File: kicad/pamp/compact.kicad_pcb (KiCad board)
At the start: 2 copper layers, 80 x 100 mm, 79 parts, among them J1 input, J2 Conn_01x02_Female, J3 output, J4 power, Q1 2SA1381F, Q10 BC546B, Q11 MJE340, Q12 2SA1381F, Q13 2SC3503F, Q14 BC546B, Q15 BC556B, Q16 IRFP240N, Q17 IRFP9240N, Q2 2SC3503F, Q3 2SA1381F, Q4 2SC3503F, Q5 BC550C, Q6 BC560C, Q7 BC550C, Q8 BC560C, Q9 BC556B

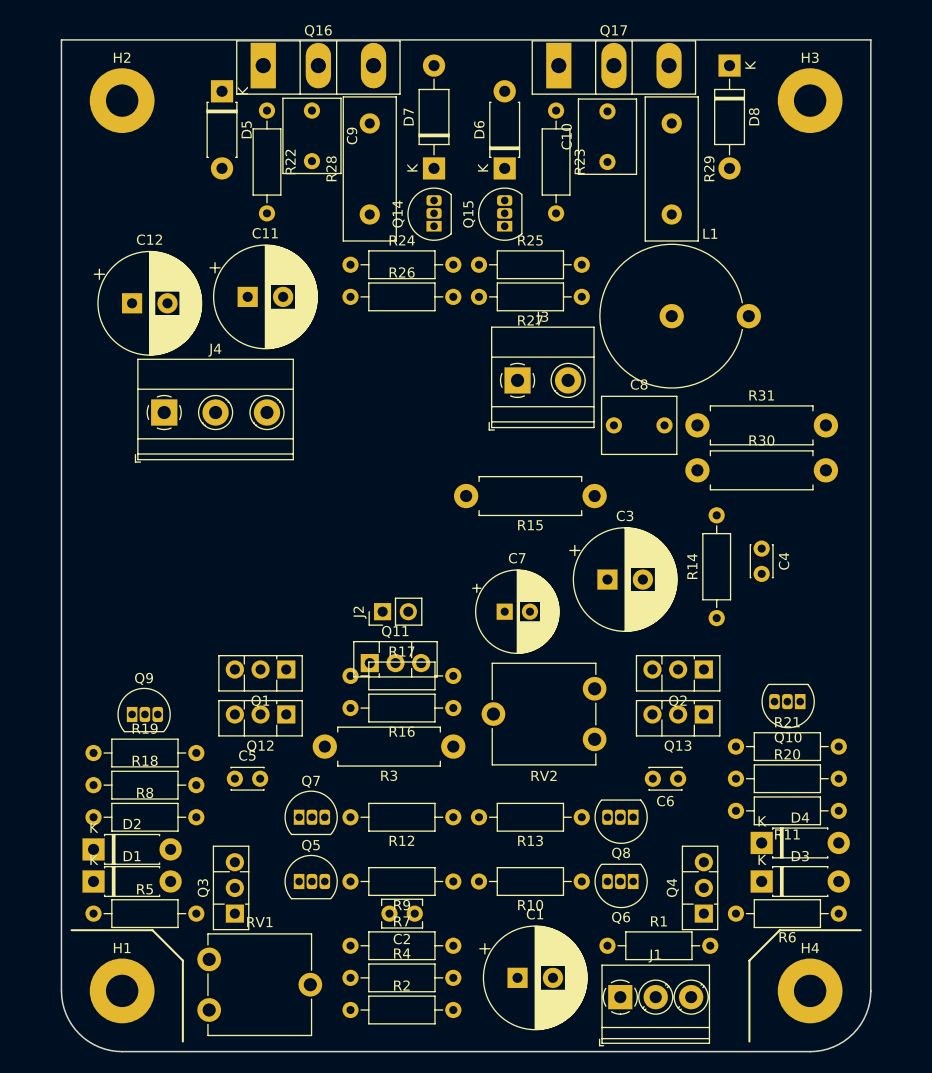
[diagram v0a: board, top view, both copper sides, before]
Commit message: Minimal PCB version.
Signed-off-by: Nenad Radulovic <nenad.b.radulovic@gmail.com>
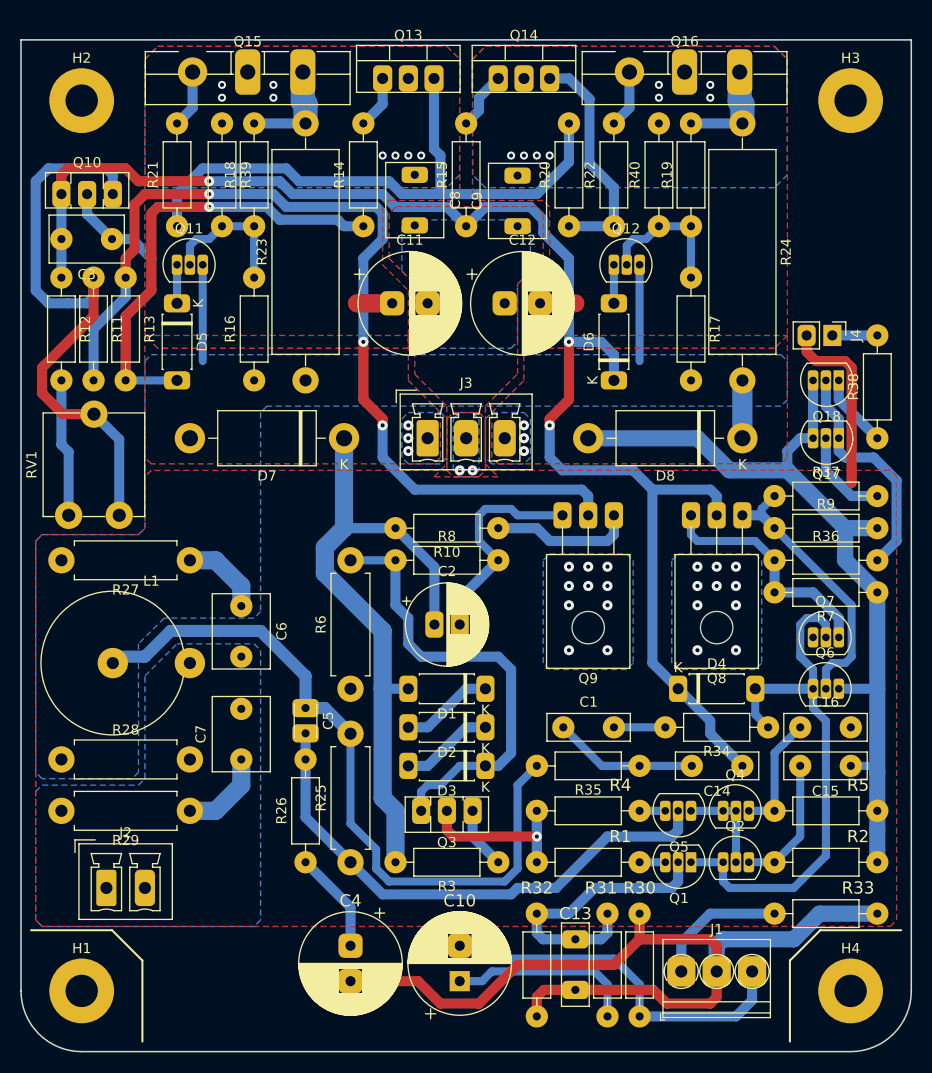
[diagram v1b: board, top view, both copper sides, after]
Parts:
- removed the C4 at (139.2, 80.3)
- removed the Q1 at (92.2, 92.2)
- removed the Q11 at (100.5, 91.6)
- removed the Q12 at (92.2, 96.7)
- removed the Q5 at (93.5, 113.2)
- removed the RV1 at (84.6, 125.9)
- added C13: 470p, Capacitor_THT:C_Disc_D8.0mm_W2.5mm_P5.00mm, F.Cu at (120.8, 123.9)
- added C14: 1n8, Capacitor_THT:C_Disc_D8.0mm_W2.5mm_P5.00mm, F.Cu at (137.3, 101.8)
- added C15: 220p, Capacitor_THT:C_Disc_D8.0mm_W2.5mm_P5.00mm, F.Cu at (148.0, 101.8)
- added C16: 220p, Capacitor_THT:C_Disc_D8.0mm_W2.5mm_P5.00mm, F.Cu at (143.0, 97.9)
- added C3: 220n, Capacitor_THT:C_Rect_L7.2mm_W4.5mm_P5.00mm_FKS2_FKP2_MKS2_MKP2, F.Cu at (75.0, 49.7)
- added Q14: Q_PNP_BCE, Package_TO_SOT_THT:TO-220-3_Vertical, F.Cu at (113.2, 33.8)
- added Q15: MJL3281, Package_TO_SOT_THT:TO-264-3_Vertical, F.Cu at (83.0, 33.2)
- added Q18: BC546B, Package_TO_SOT_THT:TO-92L_Inline, F.Cu at (146.8, 63.7)
- added Q6: BC546B, Package_TO_SOT_THT:TO-92L_Inline, F.Cu at (144.3, 94.1)
- added Q8: 2SC3503F, Package_TO_SOT_THT:TO-126-3_Horizontal_TabDown, F.Cu at (137.3, 77.0)
- added R32: 1k8, Resistor_THT:R_Axial_DIN0207_L6.3mm_D2.5mm_P10.16mm_Horizontal, F.Cu at (117.0, 126.5)
- added R33: 10, Resistor_THT:R_Axial_DIN0207_L6.3mm_D2.5mm_P10.16mm_Horizontal, F.Cu at (140.5, 116.4)
- added R34: 10, Resistor_THT:R_Axial_DIN0207_L6.3mm_D2.5mm_P10.16mm_Horizontal, F.Cu at (139.8, 97.9)
- added R35: 1k, Resistor_THT:R_Axial_DIN0207_L6.3mm_D2.5mm_P10.16mm_Horizontal, F.Cu at (127.1, 101.8)
- added R36: 10k, Resistor_THT:R_Axial_DIN0207_L6.3mm_D2.5mm_P10.16mm_Horizontal, F.Cu at (140.5, 81.4)
- added R37: 10k, Resistor_THT:R_Axial_DIN0207_L6.3mm_D2.5mm_P10.16mm_Horizontal, F.Cu at (140.5, 75.1)
- added R38: 10k, Resistor_THT:R_Axial_DIN0207_L6.3mm_D2.5mm_P10.16mm_Horizontal, F.Cu at (150.6, 69.4)
- added R39: 27k, Resistor_THT:R_Axial_DIN0207_L6.3mm_D2.5mm_P10.16mm_Horizontal, F.Cu at (85.9, 38.3)
- added R40: 27k, Resistor_THT:R_Axial_DIN0207_L6.3mm_D2.5mm_P10.16mm_Horizontal, F.Cu at (129.1, 48.4)
- C1: value 100u -> 180p; footprint Capacitor_THT:CP_Radial_D10.0mm_P3.50mm -> Capacitor_THT:C_Disc_D8.0mm_W2.5mm_P5.00mm
- C10: value 100n -> 100u; footprint Capacitor_THT:C_Rect_L7.2mm_W5.5mm_P5.00mm_FKS2_FKP2_MKS2_MKP2 -> Capacitor_THT:CP_Radial_D10.0mm_P3.50mm
- C2: value 470p -> 100u; footprint Capacitor_THT:C_Disc_D3.8mm_W2.6mm_P2.50mm -> Capacitor_THT:CP_Radial_D8.0mm_P2.50mm
- C5: value 47p -> 8.2p
- C6: value 47p -> 100n; footprint Capacitor_THT:C_Disc_D3.0mm_W2.0mm_P2.50mm -> Capacitor_THT:C_Rect_L7.2mm_W5.5mm_P5.00mm_FKS2_FKP2_MKS2_MKP2
- C7: value 47u -> 100n; footprint Capacitor_THT:CP_Radial_D8.0mm_P2.50mm -> Capacitor_THT:C_Rect_L7.2mm_W5.5mm_P5.00mm_FKS2_FKP2_MKS2_MKP2
- D7, D8: value ZPY12-TR -> 1N5401; footprint Diode_THT:D_DO-41_SOD81_P10.16mm_Horizontal -> Diode_THT:D_DO-201AD_P15.24mm_Horizontal
- J2: value Conn_01x02_Female -> output; footprint Connector_PinHeader_2.54mm:PinHeader_1x02_P2.54mm_Vertical -> Connector_Phoenix_MC:PhoenixContact_MCV_1,5_2-G-3.81_1x02_P3.81mm_Vertical
- J3: value output -> power; footprint TerminalBlock_Phoenix:TerminalBlock_Phoenix_MKDS-1,5-2_1x02_P5.00mm_Horizontal -> Connector_Phoenix_MC:PhoenixContact_MCV_1,5_3-G-3.81_1x03_P3.81mm_Vertical
- J4: value power -> Conn_01x02; footprint TerminalBlock_Phoenix:TerminalBlock_Phoenix_MKDS-1,5-3-5.08_1x03_P5.08mm_Horizontal -> Connector_PinHeader_2.54mm:PinHeader_1x02_P2.54mm_Vertical
- Q10: value BC546B -> MJE340; footprint Package_TO_SOT_THT:TO-92L_Inline -> Package_TO_SOT_THT:TO-126-3_Vertical
- Q13: value 2SC3503F -> 2SC4793; footprint Package_TO_SOT_THT:TO-126-3_Vertical -> Package_TO_SOT_THT:TO-220-3_Vertical
- Q16: value IRFP240N -> MJL1302; footprint Package_TO_SOT_THT:TO-247-3_Vertical -> Package_TO_SOT_THT:TO-264-3_Vertical
- Q17: value IRFP9240N -> BC546B; footprint Package_TO_SOT_THT:TO-247-3_Vertical -> Package_TO_SOT_THT:TO-92L_Inline
- Q2, Q4: value 2SC3503F -> BC550C; footprint Package_TO_SOT_THT:TO-126-3_Vertical -> Package_TO_SOT_THT:TO-92L_Inline
- Q7: value BC550C -> BC546B
- Q9: value BC556B -> 2SA1381F; footprint Package_TO_SOT_THT:TO-92L_Inline -> Package_TO_SOT_THT:TO-126-3_Horizontal_TabDown
- R1: value 10 -> 120
- R12, R4: value 100 -> 120
- R13: value 100 -> 33
- R14, R9: value 100 -> 24
- R15: value 1k5 -> 24; footprint Resistor_THT:R_Axial_DIN0411_L9.9mm_D3.6mm_P12.70mm_Horizontal -> Resistor_THT:R_Axial_DIN0207_L6.3mm_D2.5mm_P10.16mm_Horizontal
- R16: value 6k8 -> 330
- R17, R8: value 1k -> 330
- R18: value 18 -> 750
- R19: value 82 -> 750
- R2: value 10k -> 100
- R20: value 82 -> 62
- R21: value 18 -> 2R2
- R22: value 100 -> 2R2
- R23, R24: value 100 -> 0.22; footprint Resistor_THT:R_Axial_DIN0207_L6.3mm_D2.5mm_P10.16mm_Horizontal -> Resistor_THT:R_Axial_Power_L20.0mm_W6.4mm_P25.40mm
- R25: value 100 -> 1k8; footprint Resistor_THT:R_Axial_DIN0207_L6.3mm_D2.5mm_P10.16mm_Horizontal -> Resistor_THT:R_Axial_DIN0411_L9.9mm_D3.6mm_P12.70mm_Horizontal
- R27: value 100 -> 10; footprint Resistor_THT:R_Axial_DIN0207_L6.3mm_D2.5mm_P10.16mm_Horizontal -> Resistor_THT:R_Axial_DIN0411_L9.9mm_D3.6mm_P12.70mm_Horizontal
- R28: value 0.15 -> 4R7; footprint Resistor_THT:R_Box_L14.0mm_W5.0mm_P9.00mm -> Resistor_THT:R_Axial_DIN0411_L9.9mm_D3.6mm_P12.70mm_Horizontal
- R29: value 0.22 -> 10; footprint Resistor_THT:R_Box_L14.0mm_W5.0mm_P9.00mm -> Resistor_THT:R_Axial_DIN0411_L9.9mm_D3.6mm_P12.70mm_Horizontal
- R3: value 8k2 -> 330; footprint Resistor_THT:R_Axial_DIN0411_L9.9mm_D3.6mm_P12.70mm_Horizontal -> Resistor_THT:R_Axial_DIN0207_L6.3mm_D2.5mm_P10.16mm_Horizontal
- R30: value 10 -> 10k; footprint Resistor_THT:R_Axial_DIN0411_L9.9mm_D3.6mm_P12.70mm_Horizontal -> Resistor_THT:R_Axial_DIN0207_L6.3mm_D2.5mm_P10.16mm_Horizontal
- R31: value 4.7 -> 100; footprint Resistor_THT:R_Axial_DIN0411_L9.9mm_D3.6mm_P12.70mm_Horizontal -> Resistor_THT:R_Axial_DIN0207_L6.3mm_D2.5mm_P10.16mm_Horizontal
- R5: value 1k -> 100
- R6: value 560 -> 4k7; footprint Resistor_THT:R_Axial_DIN0207_L6.3mm_D2.5mm_P10.16mm_Horizontal -> Resistor_THT:R_Axial_DIN0411_L9.9mm_D3.6mm_P12.70mm_Horizontal
- R7: value 1k5 -> 910
- RV1: renamed from RV2; value R_POT_TRIM -> 500
- moved R11 90.6 mm to (73.2, 53.5), turned to 270 degrees
- moved Q10 88.6 mm to (70.0, 45.2), turned to 0 degrees
- moved R29 83.0 mm to (82.7, 106.2), turned to 180 degrees
- moved C10 82.3 mm to (109.4, 123.0)
- moved R19 78.7 mm to (132.2, 48.4), turned to 90 degrees
- moved R5 78.1 mm to (150.6, 106.2), turned to 180 degrees
- moved R21 75.5 mm to (81.4, 48.4), turned to 90 degrees
- moved Q13 70.4 mm to (101.7, 33.8), turned to 0 degrees
- moved R13 69.8 mm to (76.3, 53.5), turned to 270 degrees
- moved J4 66.5 mm to (146.2, 59.2), turned to 270 degrees
- moved R12 65.9 mm to (70.0, 53.5), turned to 270 degrees
- moved L1 65.0 mm to (75.1, 91.6)
- moved R7 62.7 mm to (150.6, 84.6), turned to 180 degrees
- moved R28 61.9 mm to (70.0, 101.1), turned to 0 degrees
- moved R25 60.4 mm to (98.6, 111.3), turned to 90 degrees
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- renumbered C3 to C4, Q6 to Q1, Q14 to Q11, Q15 to Q12, Q8 to Q5
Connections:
- C10 pad 1: GNDA -> Net-(C10-Pad1)
- C10 pad 2: VSS -> Net-(C10-Pad2)
- C2 pad 1: GNDS -> VDD
- C4 pad 1: Net-(C3-Pad1) -> Net-(C4-Pad1)
- C5 pad 2: Net-(C5-Pad2) -> inv
- C6 pad 2: Net-(C6-Pad2) -> GNDA
- C7 pad 1: Net-(C5-Pad2) -> Net-(C7-Pad1)
- C7 pad 2: Net-(C6-Pad1) -> GNDA
- C8 pad 1: Net-(C8-Pad1) -> VDD
- C9 pad 1: VDD -> GNDA
- C9 pad 2: GNDA -> VSS
- D3 pad 2: Net-(D3-Pad2) -> Net-(D2-Pad1)
- D4 pad 1: VSS -> Net-(C14-Pad1)
- D4 pad 2: Net-(D3-Pad1) -> Net-(D4-Pad2)
- D5 pad 2: Net-(C5-Pad2) -> Net-(C3-Pad1)
- D6 pad 1: Net-(C6-Pad1) -> Net-(C14-Pad1)
- D7 pad 1: Net-(D5-Pad1) -> VDD
- D7 pad 2: Net-(D7-Pad2) -> Net-(C5-Pad1)
- D8 pad 1: Net-(D8-Pad1) -> Net-(C5-Pad1)
- D8 pad 2: Net-(D6-Pad2) -> VSS
- J1 pad 3: Net-(C1-Pad2) -> Net-(C10-Pad2)
- J2 pad 2: Net-(C6-Pad1) -> GNDA
- J3 pad 1: Net-(J3-Pad1) -> VDD
- J4 pad 1: VDD -> Net-(J4-Pad1)
- L1 pad 1: Net-(C4-Pad1) -> Net-(C5-Pad1)
- L1 pad 2: Net-(J3-Pad1) -> Net-(J2-Pad1)
- Q1 pad 1: Net-(C6-Pad2) -> Net-(D4-Pad2)
- Q1 pad 2: Net-(C2-Pad2) -> ninv
- Q1 pad 3: Net-(Q6-Pad3) -> Net-(Q1-Pad3)
- Q10 pad 1: Net-(C6-Pad2) -> Net-(C14-Pad1)
- Q10 pad 2: Net-(Q10-Pad2) -> Net-(C3-Pad1)
- Q10 pad 3: VSS -> Net-(Q10-Pad3)
- Q11 pad 2: Net-(Q14-Pad2) -> Net-(Q11-Pad2)
- Q11 pad 3: Net-(C4-Pad1) -> Net-(C5-Pad1)
- Q12 pad 2: Net-(Q15-Pad2) -> Net-(Q12-Pad2)
- Q12 pad 3: Net-(C4-Pad1) -> Net-(C5-Pad1)
- Q13 pad 2: Net-(C6-Pad1) -> VDD
- Q13 pad 3: Net-(C6-Pad2) -> Net-(Q13-Pad3)
- Q16 pad 2: VDD -> VSS
- Q16 pad 3: Net-(D7-Pad2) -> Net-(Q16-Pad3)
- Q17 pad 2: VSS -> Net-(Q17-Pad2)
- Q17 pad 3: Net-(D8-Pad1) -> VSS
- Q2 pad 1: Net-(D3-Pad2) -> Net-(D4-Pad2)
- Q2 pad 3: Net-(Q2-Pad3) -> Net-(C15-Pad2)
- Q3 pad 1: Net-(Q1-Pad3) -> Net-(Q3-Pad1)
- Q3 pad 3: Net-(Q1-Pad2) -> Net-(D3-Pad1)
- Q4 pad 1: Net-(Q2-Pad3) -> Net-(Q2-Pad2)
- Q4 pad 2: Net-(Q4-Pad2) -> Net-(Q2-Pad2)
- Q4 pad 3: Net-(Q2-Pad2) -> Net-(C16-Pad1)
- Q5 pad 1: VSS -> Net-(Q2-Pad2)
- Q5 pad 2: Net-(C4-Pad2) -> inv
- Q5 pad 3: Net-(Q8-Pad3) -> Net-(Q5-Pad3)
- Q7 pad 1: VDD -> GNDA
- Q7 pad 2: Net-(C4-Pad2) -> Net-(D4-Pad2)
- Q9 pad 1: Net-(C5-Pad1) -> Net-(Q9-Pad1)
- Q9 pad 3: VDD -> Net-(C2-Pad2)
- R1 pad 1: GNDA -> Net-(Q1-Pad3)
- R1 pad 2: GNDS -> Net-(Q3-Pad2)
- R10 pad 1: Net-(Q6-Pad3) -> Net-(Q9-Pad1)
- R10 pad 2: Net-(Q3-Pad2) -> VDD
- R11 pad 1: VSS -> Net-(Q10-Pad3)
- R11 pad 2: Net-(C6-Pad2) -> Net-(Q9-Pad2)
- R12 pad 1: Net-(Q4-Pad2) -> Net-(C14-Pad1)
- R12 pad 2: Net-(Q7-Pad3) -> Net-(R12-Pad2)
- R13 pad 1: Net-(Q8-Pad3) -> Net-(Q9-Pad2)
- R13 pad 2: Net-(Q3-Pad2) -> Net-(C3-Pad1)
- R14 pad 1: Net-(C4-Pad2) -> Net-(C3-Pad1)
- R14 pad 2: Net-(C3-Pad1) -> Net-(Q13-Pad1)
- R15 pad 1: Net-(C4-Pad2) -> Net-(C14-Pad1)
- R15 pad 2: Net-(C4-Pad1) -> Net-(Q14-Pad1)
- R16 pad 1: Net-(Q11-Pad3) -> Net-(C5-Pad1)
- R16 pad 2: Net-(C5-Pad2) -> Net-(Q11-Pad2)
- R17 pad 1: Net-(C6-Pad1) -> Net-(Q12-Pad2)
- R17 pad 2: Net-(R17-Pad2) -> Net-(C5-Pad1)
- R18 pad 1: Net-(Q9-Pad2) -> Net-(Q11-Pad2)
- R18 pad 2: VDD -> Net-(Q15-Pad3)
- R19 pad 1: Net-(Q12-Pad1) -> Net-(Q12-Pad2)
- R19 pad 2: Net-(Q9-Pad2) -> Net-(Q16-Pad3)
- R2 pad 1: GNDS -> VSS
- R2 pad 2: Net-(C1-Pad2) -> Net-(C15-Pad2)
- R20 pad 1: Net-(Q10-Pad2) -> Net-(Q14-Pad3)
- R20 pad 2: Net-(Q13-Pad1) -> Net-(Q13-Pad3)
- R21 pad 1: VSS -> Net-(Q13-Pad3)
- R21 pad 2: Net-(Q10-Pad2) -> Net-(Q15-Pad1)
- R22 pad 1: Net-(Q16-Pad1) -> Net-(Q14-Pad3)
- R22 pad 2: Net-(C5-Pad2) -> Net-(Q16-Pad1)
- R23 pad 1: Net-(Q17-Pad1) -> Net-(C5-Pad1)
- R23 pad 2: Net-(C6-Pad1) -> Net-(Q15-Pad3)
- R24 pad 1: Net-(C4-Pad1) -> Net-(Q16-Pad3)
- R24 pad 2: Net-(Q14-Pad2) -> Net-(C5-Pad1)
- R25 pad 1: Net-(Q15-Pad2) -> inv
- R25 pad 2: Net-(C4-Pad1) -> Net-(C5-Pad1)
- R26 pad 1: Net-(D7-Pad2) -> Net-(C4-Pad1)
- R26 pad 2: Net-(Q14-Pad2) -> inv
- R27 pad 1: Net-(D8-Pad1) -> Net-(C6-Pad1)
- R27 pad 2: Net-(Q15-Pad2) -> Net-(C5-Pad1)
- R28 pad 1: Net-(C4-Pad1) -> Net-(C5-Pad1)
- R28 pad 2: Net-(D7-Pad2) -> Net-(J2-Pad1)
- R29 pad 1: Net-(D8-Pad1) -> Net-(C7-Pad1)
- R29 pad 2: Net-(C4-Pad1) -> Net-(J2-Pad1)
- R3 pad 1: Net-(Q2-Pad2) -> Net-(Q3-Pad1)
- R3 pad 2: Net-(Q1-Pad2) -> VDD
- R30 pad 1: Net-(C8-Pad1) -> GNDS
- R30 pad 2: Net-(C4-Pad1) -> Net-(C10-Pad2)
- R31 pad 1: Net-(C4-Pad1) -> Net-(C10-Pad1)
- R31 pad 2: Net-(J3-Pad1) -> ninv
- R4 pad 1: Net-(C2-Pad2) -> Net-(Q5-Pad3)
- R4 pad 2: Net-(C1-Pad1) -> Net-(Q3-Pad2)
- R5 pad 1: Net-(Q1-Pad3) -> VSS
- R5 pad 2: Net-(R5-Pad2) -> Net-(C16-Pad1)
- R6 pad 1: VSS -> GNDA
- R6 pad 2: Net-(Q2-Pad3) -> Net-(D3-Pad1)
- R7 pad 1: Net-(C2-Pad2) -> VSS
- R7 pad 2: GNDS -> Net-(Q7-Pad3)
- R8 pad 1: Net-(C5-Pad1) -> Net-(D3-Pad1)
- R8 pad 2: VDD -> Net-(C2-Pad2)
- R9 pad 1: Net-(Q4-Pad2) -> Net-(Q6-Pad2)
- R9 pad 2: Net-(Q5-Pad3) -> VSS
- RV1 pad 1: Net-(Q11-Pad3) -> Net-(Q10-Pad3)
- RV1 pad 2: Net-(Q11-Pad3) -> Net-(Q10-Pad3)
- RV1 pad 3: Net-(R17-Pad2) -> Net-(R12-Pad2)
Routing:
- net Net-(C14-Pad1): track 0.00 -> 145.6 mm, vias 0 -> 3
- net Net-(C5-Pad1): track 0.00 -> 95.7 mm
- net Net-(Q9-Pad2): track 0.00 -> 94.3 mm, vias 0 -> 3
- net GNDS: track 0.00 -> 88.2 mm
- net VSS: track 0.00 -> 87.2 mm, vias 0 -> 11
- net Net-(C3-Pad1): track 0.00 -> 67.9 mm, vias 0 -> 1
- net VDD: track 0.00 -> 67.8 mm, vias 0 -> 11
- net Net-(Q13-Pad3): track 0.00 -> 60.8 mm
- net Net-(Q10-Pad3): track 0.00 -> 60.1 mm
- net Net-(D4-Pad2): track 0.00 -> 55.1 mm
- net inv: track 0.00 -> 52.8 mm
- net Net-(D3-Pad1): track 0.00 -> 45.1 mm
- net Net-(C10-Pad2): track 0.00 -> 37.2 mm
- net GNDA: track 0.00 -> 31.4 mm, vias 0 -> 22
- net ninv: track 0.00 -> 28.5 mm
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- added copper zone on B.Cu, net GNDA
- added copper zone on F.Cu, net GNDA
- added copper zone on B.Cu, net Net-(C5-Pad1)
- added copper zone on B.Cu, net Net-(J2-Pad1)
- added copper zone on B.Cu, net VDD
- added copper zone on F.Cu, net VDD
- added copper zone on B.Cu, net VSS
- added copper zone on F.Cu, net VSS
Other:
- board size 80 x 100 mm -> 88 x 100 mm
- net class Default: clearance 0.2 -> 0.2032; trace_width 0.25 -> 0.3; via_dia 0.8 -> 1
- rule trace_clearance: 0.2 -> 0.2032
- rule trace_min: 0.2 -> 0.3

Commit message: First prerelease.
Signed-off-by: Nenad Radulovic <nenad.b.radulovic@gmail.com>
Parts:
- removed the C1 at (119.6, 97.9)
- removed the C14 at (137.3, 101.8)
- removed the C16 at (143.0, 97.9)
- removed Q17, Q18: BC546B, Package_TO_SOT_THT:TO-92L_Inline
- removed the R12 at (70.0, 53.5)
- removed the R17 at (132.2, 53.5)
- removed the R18 at (89.0, 48.4)
- removed the R19 at (132.2, 48.4)
- removed the R23 at (94.1, 63.7)
- removed the R34 at (139.8, 97.9)
- removed R35: 1k, Resistor_THT:R_Axial_DIN0207_L6.3mm_D2.5mm_P10.16mm_Horizontal
- removed R39, R40: 27k, Resistor_THT:R_Axial_DIN0207_L6.3mm_D2.5mm_P10.16mm_Horizontal
- added C2: 220p, Capacitor_THT:C_Disc_D8.0mm_W2.5mm_P5.00mm, F.Cu at (143.1, 99.8)
- added C3: 180p, Capacitor_THT:C_Disc_D8.0mm_W2.5mm_P5.00mm, F.Cu at (125.2, 88.4)
- added C5: 1n8, Capacitor_THT:C_Disc_D8.0mm_W2.5mm_P5.00mm, F.Cu at (125.2, 78.3)
- added D6: BAV21, Diode_THT:D_DO-41_SOD81_P7.62mm_Horizontal, F.Cu at (89.0, 59.2)
- added D7: BAV21, Diode_THT:D_DO-41_SOD81_P7.62mm_Horizontal, F.Cu at (124.6, 59.2)
- added LOGO1: Logo_Open_Hardware_Small, Symbol:KiCad-Logo_5mm_Copper, F.Cu at (86.0, 123.0)
- added R11: 1k, Resistor_THT:R_Axial_DIN0207_L6.3mm_D2.5mm_P10.16mm_Horizontal, F.Cu at (126.5, 97.9)
- added R25: 0.22, Resistor_THT:R_Axial_Power_L20.0mm_W6.4mm_P25.40mm, F.Cu at (137.3, 38.3)
- added R7: 10, Resistor_THT:R_Axial_DIN0207_L6.3mm_D2.5mm_P10.16mm_Horizontal, F.Cu at (139.8, 97.9)
- Q1, Q11, Q2, Q4, Q5, Q6, Q7: footprint Package_TO_SOT_THT:TO-92L_Inline -> Package_TO_SOT_THT:TO-92L_Inline_Wide
- Q12: value BC556B -> BC546B; footprint Package_TO_SOT_THT:TO-92L_Inline -> Package_TO_SOT_THT:TO-92L_Inline_Wide
- R16: value 330 -> 120
- moved Q11 68.8 mm to (148.1, 69.4), turned to 180 degrees
- moved R24 50.1 mm to (94.1, 63.7), turned to 90 degrees
- moved Q12 26.1 mm to (148.1, 63.7), turned to 180 degrees
- moved R16 21.6 mm to (70.0, 53.5), turned to 270 degrees
- moved D4 16.1 mm to (128.4, 78.3), turned to 270 degrees
- moved D8 12.7 mm to (132.2, 53.5), turned to 180 degrees
- moved R18 10.2 mm to (150.6, 59.2)
- moved C1 5.72 mm to (148.0, 107.5)
- moved Q9 3.42 mm to (121.4, 78.3)
- moved Q1 2.84 mm to (131.0, 113.8), turned to 90 degrees
- moved R4 2.62 mm to (126.5, 103.7)
- moved Q2 2.62 mm to (136.0, 113.8), turned to 90 degrees
- moved R5 2.54 mm to (150.6, 103.7)
- moved D5 2.54 mm to (81.4, 53.5), turned to 0 degrees
- moved Q8 1.27 mm to (137.3, 78.3)
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- renumbered C15 to C1, C7 to C10, C8 to C11, C9 to C12, C10 to C13, C11 to C14, C12 to C15, C13 to C16, C2 to C4, C3 to C6, C4 to C7, C5 to C8, C6 to C9, D8 to D10, D6 to D8, D7 to D9, J4 to J1, J1 to J2, J2 to J3, J3 to J4, R9 to R10, R36 to R12, R37 to R13, R10 to R14, R11 to R15, R13 to R17, R38 to R18, R14 to R19, R15 to R20, R20 to R21, R21 to R22, R22 to R23, R25 to R26, R26 to R27, R27 to R28, R28 to R29, R29 to R30, R30 to R31, R31 to R32, R32 to R33, R33 to R34, R7 to R8, R8 to R9
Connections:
- C6 pad 1: Net-(C3-Pad1) -> Net-(C6-Pad1)
- C6 pad 2: Net-(C14-Pad1) -> Net-(C5-Pad1)
- C8 pad 1: Net-(C5-Pad1) -> Net-(C8-Pad1)
- D10 pad 1: Net-(C5-Pad1) -> Net-(C8-Pad1)
- D4 pad 1: Net-(C14-Pad1) -> Net-(C5-Pad1)
- D5 pad 1: Net-(D5-Pad1) -> Net-(C6-Pad1)
- D5 pad 2: Net-(C3-Pad1) -> Net-(D5-Pad2)
- D8 pad 1: Net-(C14-Pad1) -> Net-(D7-Pad2)
- D8 pad 2: Net-(D6-Pad2) -> Net-(C5-Pad1)
- D9 pad 2: Net-(C5-Pad1) -> Net-(C8-Pad1)
- L1 pad 1: Net-(C5-Pad1) -> Net-(C8-Pad1)
- Q10 pad 1: Net-(C14-Pad1) -> Net-(C5-Pad1)
- Q10 pad 2: Net-(C3-Pad1) -> Net-(C6-Pad1)
- Q11 pad 1: Net-(D5-Pad1) -> Net-(Q11-Pad1)
- Q11 pad 3: Net-(C5-Pad1) -> VSS
- Q12 pad 1: Net-(D6-Pad2) -> Net-(Q12-Pad1)
- Q12 pad 2: Net-(Q12-Pad2) -> Net-(Q11-Pad1)
- Q12 pad 3: Net-(C5-Pad1) -> VSS
- Q8 pad 2: Net-(C14-Pad1) -> Net-(C5-Pad1)
- R12 pad 2: Net-(Q17-Pad1) -> Net-(Q11-Pad1)
- R13 pad 2: Net-(Q17-Pad2) -> Net-(Q11-Pad2)
- R16 pad 2: Net-(Q11-Pad2) -> Net-(R16-Pad2)
- R17 pad 2: Net-(C3-Pad1) -> Net-(C6-Pad1)
- R18 pad 1: Net-(Q18-Pad1) -> Net-(Q12-Pad1)
- R19 pad 1: Net-(C3-Pad1) -> Net-(C6-Pad1)
- R20 pad 1: Net-(C14-Pad1) -> Net-(C5-Pad1)
- R24 pad 1: Net-(Q16-Pad3) -> Net-(C8-Pad1)
- R24 pad 2: Net-(C5-Pad1) -> Net-(Q15-Pad3)
- R26 pad 2: Net-(C5-Pad1) -> Net-(C8-Pad1)
- R28 pad 2: Net-(C5-Pad1) -> Net-(C8-Pad1)
- R29 pad 1: Net-(C5-Pad1) -> Net-(C8-Pad1)
- RV1 pad 3: Net-(R12-Pad2) -> Net-(R16-Pad2)
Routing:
- net Net-(C14-Pad1): track 145.6 -> 0.00 mm, vias 3 -> 0
- net Net-(C8-Pad1): track 0.00 -> 89.3 mm
- net Net-(C3-Pad1): track 67.9 -> 16.8 mm, vias 1 -> 0
- net Net-(C6-Pad1): track 0.00 -> 50.5 mm
- net Net-(Q17-Pad1): track 23.1 -> 0.00 mm
- net Net-(C5-Pad1): track 95.7 -> 118.8 mm, vias 0 -> 2
- net Net-(Q11-Pad1): track 0.00 -> 21.7 mm
- net Net-(D4-Pad2): track 55.1 -> 72.7 mm
- net Net-(C1-Pad1): track 14.3 -> 0.00 mm
- net Net-(Q12-Pad2): track 14.1 -> 0.00 mm
- net Net-(R16-Pad2): track 0.00 -> 13.6 mm
- net Net-(R12-Pad2): track 13.6 -> 0.00 mm
- net Net-(Q17-Pad2): track 9.31 -> 0.00 mm
- net Net-(C4-Pad2): track 21.9 -> 13.5 mm
- net Net-(J1-Pad1): track 4.44 -> 12.0 mm
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- added copper zone on B.Cu, net Net-(C8-Pad1)
- removed copper zone on B.Cu, net Net-(C5-Pad1)
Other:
- outline, holes or cut-outs redrawn
- board text added: "REAL TIME CONSULTING"

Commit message: Made the compensation scheme much simpler.
Signed-off-by: Nenad Radulovic <nenad.b.radulovic@gmail.com>
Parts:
- removed C5: 1n8, Capacitor_THT:C_Disc_D8.0mm_W2.5mm_P5.00mm
- removed R11: 1k, Resistor_THT:R_Axial_DIN0207_L6.3mm_D2.5mm_P10.16mm_Horizontal
- removed R7: 10, Resistor_THT:R_Axial_DIN0207_L6.3mm_D2.5mm_P10.16mm_Horizontal
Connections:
- C6 pad 2: Net-(C5-Pad1) -> Net-(C3-Pad1)
- D4 pad 1: Net-(C5-Pad1) -> Net-(C3-Pad1)
- D4 pad 2: Net-(D4-Pad2) -> Net-(C3-Pad2)
- D8 pad 2: Net-(C5-Pad1) -> Net-(C3-Pad1)
- Q1 pad 1: Net-(D4-Pad2) -> Net-(C3-Pad2)
- Q10 pad 1: Net-(C5-Pad1) -> Net-(C3-Pad1)
- Q2 pad 1: Net-(D4-Pad2) -> Net-(C3-Pad2)
- Q6 pad 1: Net-(D4-Pad2) -> Net-(C3-Pad2)
- Q7 pad 2: Net-(D4-Pad2) -> Net-(C3-Pad2)
- Q8 pad 2: Net-(C5-Pad1) -> Net-(C3-Pad1)
- R16 pad 1: Net-(C5-Pad1) -> Net-(C3-Pad1)
- R20 pad 1: Net-(C5-Pad1) -> Net-(C3-Pad1)
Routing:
- net Net-(C5-Pad1): track 118.8 -> 0.00 mm, vias 2 -> 0
- net Net-(C3-Pad1): track 16.8 -> 127.1 mm, vias 0 -> 2
- net Net-(D4-Pad2): track 72.7 -> 0.00 mm
- net Net-(C3-Pad2): track 6.37 -> 75.9 mm
- net Net-(C8-Pad1): track 89.3 -> 41.0 mm
